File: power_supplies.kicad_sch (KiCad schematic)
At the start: 55 parts, among them IC1 ECP5-BGA256, Q16 2NPN, U15 1V8REG, U3 3V3REG, U4 1V15REG, U5 2V5REG

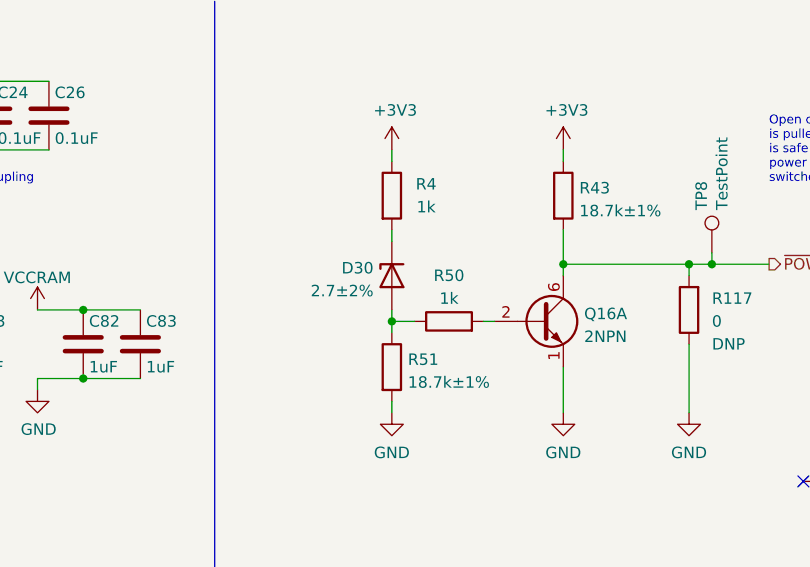
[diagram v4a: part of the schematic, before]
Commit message: Tune POWER_GOOD detection
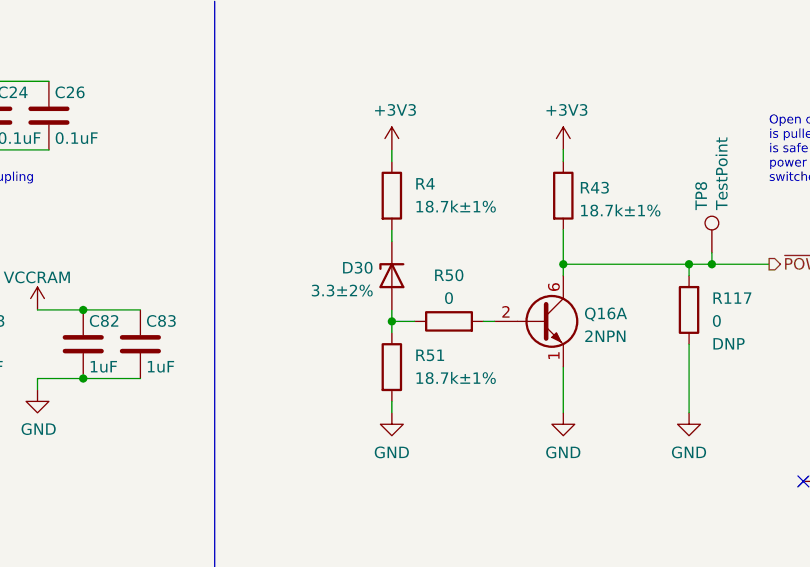
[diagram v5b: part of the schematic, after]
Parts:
- D30: value 2.7±2% -> 3.3±2%; Part Number BZX884-B2V7,315 -> BZX884-B3V3,315
- R4: value 1k -> 18.7k±1%; Manufacturer Yageo -> Panasonic; Part Number RC0402JR-071KL -> ERJ-2RKF1872X
- R50: value 1k -> 0; Part Number RC0402JR-071KL -> RC0402FR-070RL
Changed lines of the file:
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@@
       (effects (font (size 1.27 1.27)))
     )
-    (property "Value" "1k" (at 168.91 45.72 90)
+    (property "Value" "0" (at 168.91 45.72 90)
       (effects (font (size 1.27 1.27)))
     )
@@
       (effects (font (size 1.27 1.27)) hide)
     )
-    (property "Part Number" "RC0402JR-071KL" (at 168.91 48.26 0)
+    (property "Part Number" "RC0402FR-070RL" (at 168.91 48.26 0)
       (effects (font (size 1.27 1.27)) hide)
     )
@@
       (effects (font (size 1.27 1.27)) hide)
     )
-    (property "Description" "RES 1K OHM 5% 1/16W 0402" (at 168.91 48.26 0)
+    (property "Description" "RES 0 OHM JUMPER 1/16W 0402" (at 168.91 48.26 0)
       (effects (font (size 1.27 1.27)) hide)
     )
@@
       (effects (font (size 1.27 1.27)) (justify left))
     )
-    (property "Value" "2.7±2%" (at 160.528 44.8822 90)
+    (property "Value" "3.3±2%" (at 160.528 44.8822 90)
       (effects (font (size 1.27 1.27)) (justify left))
     )
@@
       (effects (font (size 1.27 1.27)) hide)
     )
-    (property "Part Number" "BZX884-B2V7,315" (at 162.56 43.18 90)
-      (effects (font (size 1.27 1.27)) hide)
-    )
-    (property "Description" "DIODE ZENER 2.7V 250MW DFN1006-2" (at 162.56 43.18 0)
+    (property "Part Number" "BZX884-B3V3,315" (at 162.56 43.18 90)
+      (effects (font (size 1.27 1.27)) hide)
+    )
+    (property "Description" "DIODE ZENER 3.3V 250MW DFN1006-2" (at 162.56 43.18 0)
       (effects (font (size 1.27 1.27)) hide)
     )
@@
   (symbol (lib_id "Device:R") (at 162.56 34.29 0) (unit 1)
     (in_bom yes) (on_board yes) (dnp no)
-    (property "Reference" "R4" (at 166.37 33.02 0)
-      (effects (font (size 1.27 1.27)))
-    )
-    (property "Value" "1k" (at 166.37 35.56 0)
-      (effects (font (size 1.27 1.27)))
+    (property "Reference" "R4" (at 165.1 33.02 0)
+      (effects (font (size 1.27 1.27)) (justify left))
+    )
+    (property "Value" "18.7k±1%" (at 165.1 35.56 0)
+      (effects (font (size 1.27 1.27)) (justify left))
     )
     (property "Footprint" "Resistor_SMD:R_0402_1005Metric" (at 160.782 34.29 90)
@@
       (effects (font (size 1.27 1.27)) hide)
     )
-    (property "Part Number" "RC0402JR-071KL" (at 162.56 34.29 0)
+    (property "Part Number" "ERJ-2RKF1872X" (at 162.56 34.29 0)
       (effects (font (size 1.27 1.27)) hide)
     )
@@
       (effects (font (size 1.27 1.27)) hide)
     )
-    (property "Description" "RES 1K OHM 5% 1/16W 0402" (at 162.56 34.29 0)
-      (effects (font (size 1.27 1.27)) hide)
-    )
-    (property "Manufacturer" "Yageo" (at 162.56 34.29 0)
+    (property "Description" "RES SMD 18.7K OHM 1% 1/10W 0402" (at 162.56 34.29 0)
+      (effects (font (size 1.27 1.27)) hide)
+    )
+    (property "Manufacturer" "Panasonic" (at 162.56 34.29 0)
       (effects (font (size 1.27 1.27)) hide)
     )
@@
   (symbol (lib_id "Device:R") (at 162.56 53.34 0) (unit 1)
     (in_bom yes) (on_board yes) (dnp no)
-    (property "Reference" "R51" (at 164.338 52.5053 0)
-      (effects (font (size 1.27 1.27)) (justify left))
-    )
-    (property "Value" "18.7k±1%" (at 164.338 55.0422 0)
-      (effects (font (size 1.27 1.27)) (justify left))
-    )
+    (property "Reference" "R51" (at 165.1 52.07 0)
+      (effects (font (size 1.27 1.27)) (justify left))
+    )
+    (property "Value" "18.7k±1%" (at 165.1 54.61 0)
+      (effects (font (size 1.27 1.27)) (justify left))
+    )

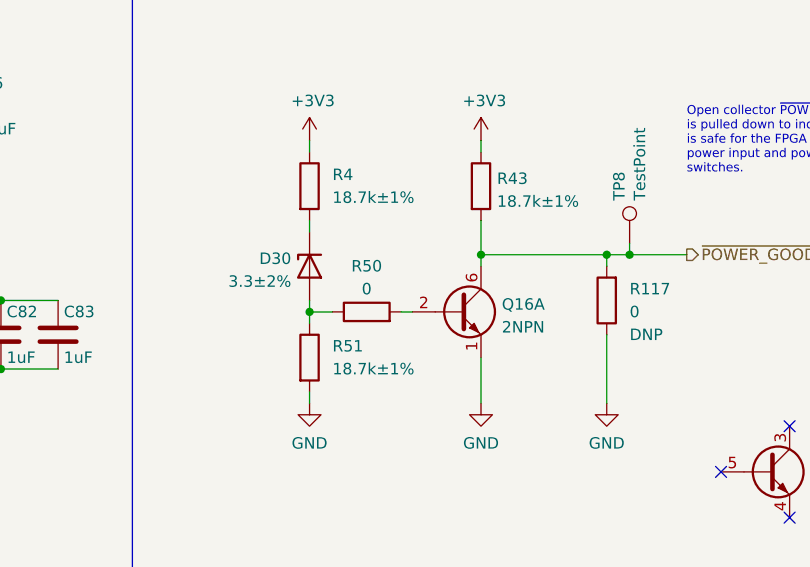
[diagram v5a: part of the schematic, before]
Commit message: Increase POWER_GOOD detection current
This helps ensure that POWER_GOOD is pulled down with sufficient
strength.
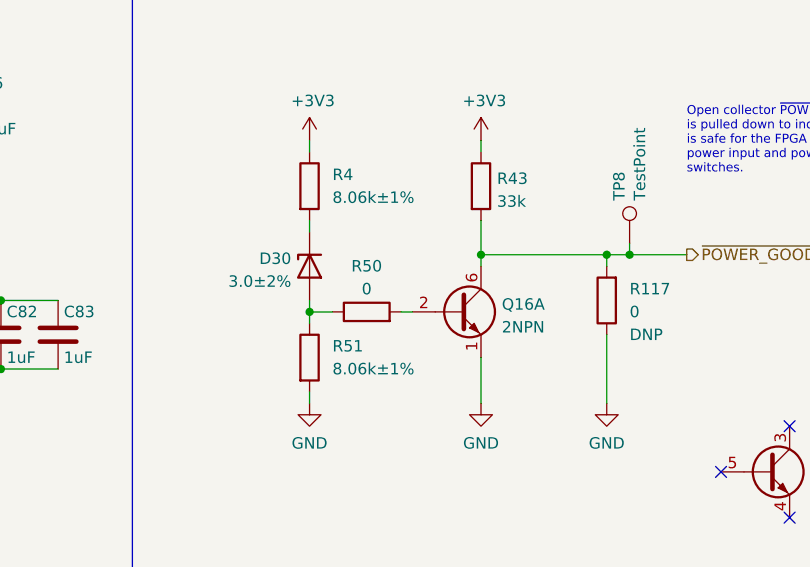
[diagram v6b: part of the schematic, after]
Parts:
- D30: value 3.3±2% -> 3.0±2%; Part Number BZX884-B3V3,315 -> BZX884-B3V0,315
- R4, R51: value 18.7k±1% -> 8.06k±1%; Part Number ERJ-2RKF1872X -> ERJ-2RKF8061X
- R43: value 18.7k±1% -> 33k; Part Number ERJ-2RKF1872X -> ERJ-2GEJ333X
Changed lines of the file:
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@@
       (effects (font (size 1.27 1.27)) (justify left))
     )
-    (property "Value" "3.3±2%" (at 160.528 44.8822 90)
+    (property "Value" "3.0±2%" (at 160.528 44.8822 90)
       (effects (font (size 1.27 1.27)) (justify left))
     )
@@
       (effects (font (size 1.27 1.27)) hide)
     )
-    (property "Part Number" "BZX884-B3V3,315" (at 162.56 43.18 90)
-      (effects (font (size 1.27 1.27)) hide)
-    )
-    (property "Description" "DIODE ZENER 3.3V 250MW DFN1006-2" (at 162.56 43.18 0)
+    (property "Part Number" "BZX884-B3V0,315" (at 162.56 43.18 90)
+      (effects (font (size 1.27 1.27)) hide)
+    )
+    (property "Description" "DIODE ZENER 3V 250MW DFN1006-2" (at 162.56 43.18 0)
       (effects (font (size 1.27 1.27)) hide)
     )
@@
       (effects (font (size 1.27 1.27)) (justify left))
     )
-    (property "Value" "18.7k±1%" (at 165.1 35.56 0)
+    (property "Value" "8.06k±1%" (at 165.1 35.56 0)
       (effects (font (size 1.27 1.27)) (justify left))
     )
@@
       (effects (font (size 1.27 1.27)) hide)
     )
-    (property "Part Number" "ERJ-2RKF1872X" (at 162.56 34.29 0)
+    (property "Part Number" "ERJ-2RKF8061X" (at 162.56 34.29 0)
       (effects (font (size 1.27 1.27)) hide)
     )
@@
       (effects (font (size 1.27 1.27)) hide)
     )
-    (property "Description" "RES SMD 18.7K OHM 1% 1/10W 0402" (at 162.56 34.29 0)
+    (property "Description" "RES SMD 8.06K OHM 1% 1/10W 0402" (at 162.56 34.29 0)
       (effects (font (size 1.27 1.27)) hide)
     )
@@
       (effects (font (size 1.27 1.27)) (justify left))
     )
-    (property "Value" "18.7k±1%" (at 165.1 54.61 0)
+    (property "Value" "8.06k±1%" (at 165.1 54.61 0)
       (effects (font (size 1.27 1.27)) (justify left))
     )
@@
       (effects (font (size 1.27 1.27)) hide)
     )
-    (property "Description" "RES SMD 18.7K OHM 1% 1/10W 0402" (at 162.56 53.34 0)
+    (property "Description" "RES SMD 8.06K OHM 1% 1/10W 0402" (at 162.56 53.34 0)
       (effects (font (size 1.27 1.27)) hide)
     )
@@
       (effects (font (size 1.27 1.27)) hide)
     )
-    (property "Part Number" "ERJ-2RKF1872X" (at 162.56 53.34 0)
+    (property "Part Number" "ERJ-2RKF8061X" (at 162.56 53.34 0)
       (effects (font (size 1.27 1.27)) hide)
     )
@@
       (effects (font (size 1.27 1.27)) (justify left))
     )
-    (property "Value" "18.7k±1%" (at 183.388 35.9922 0)
+    (property "Value" "33k" (at 183.388 35.9922 0)
       (effects (font (size 1.27 1.27)) (justify left))
     )
@@
       (effects (font (size 1.27 1.27)) hide)
     )
-    (property "Description" "RES SMD 18.7K OHM 1% 1/10W 0402" (at 181.61 34.29 0)
+    (property "Description" "RES SMD 33K OHM 5% 1/10W 0402" (at 181.61 34.29 0)
       (effects (font (size 1.27 1.27)) hide)
     )
@@
       (effects (font (size 1.27 1.27)) hide)
     )
-    (property "Part Number" "ERJ-2RKF1872X" (at 181.61 34.29 0)
-      (effects (font (size 1.27 1.27)) hide)
-    )
+    (property "Part Number" "ERJ-2GEJ333X" (at 181.61 34.29 0)
+      (effects (font (size 1.27 1.27)) hide)
+    )

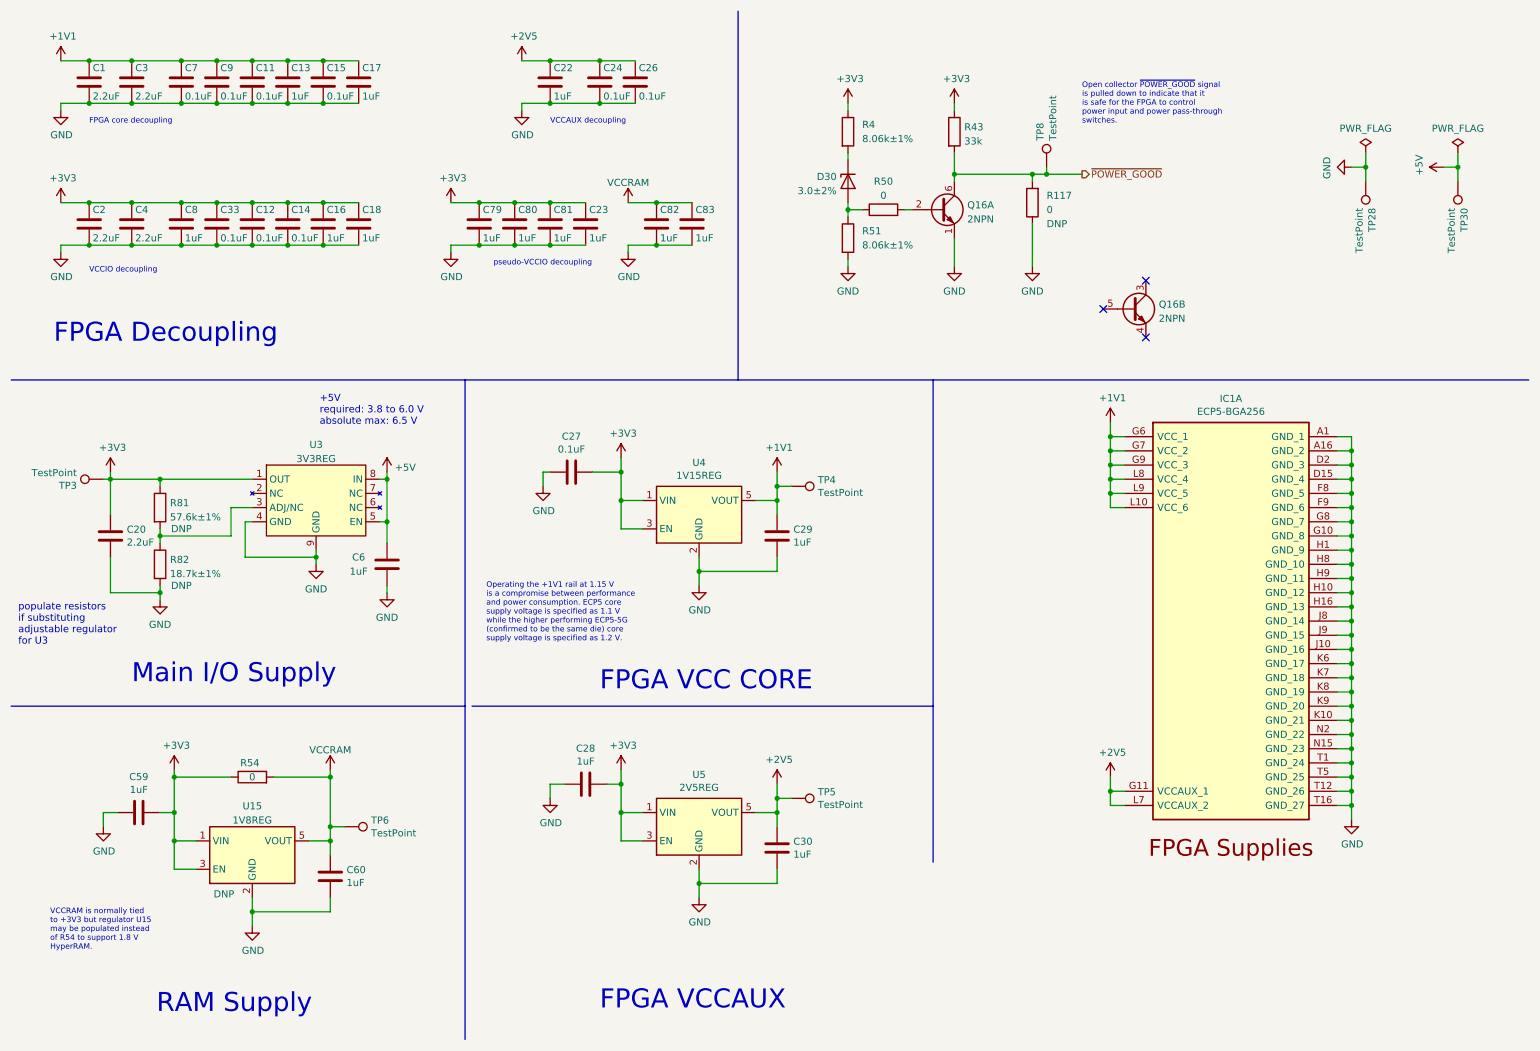
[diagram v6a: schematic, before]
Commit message: Clean up schematic
- Renumber Pmod signal names to match silkscreen labels
- Clean up FPGA symbol
- Clean up PHY symbol
- Add title block to newer sheets
- Fix horizontal line in LED sheet
- Improve various label positions
- Update data sheet fields
- Renumber pages
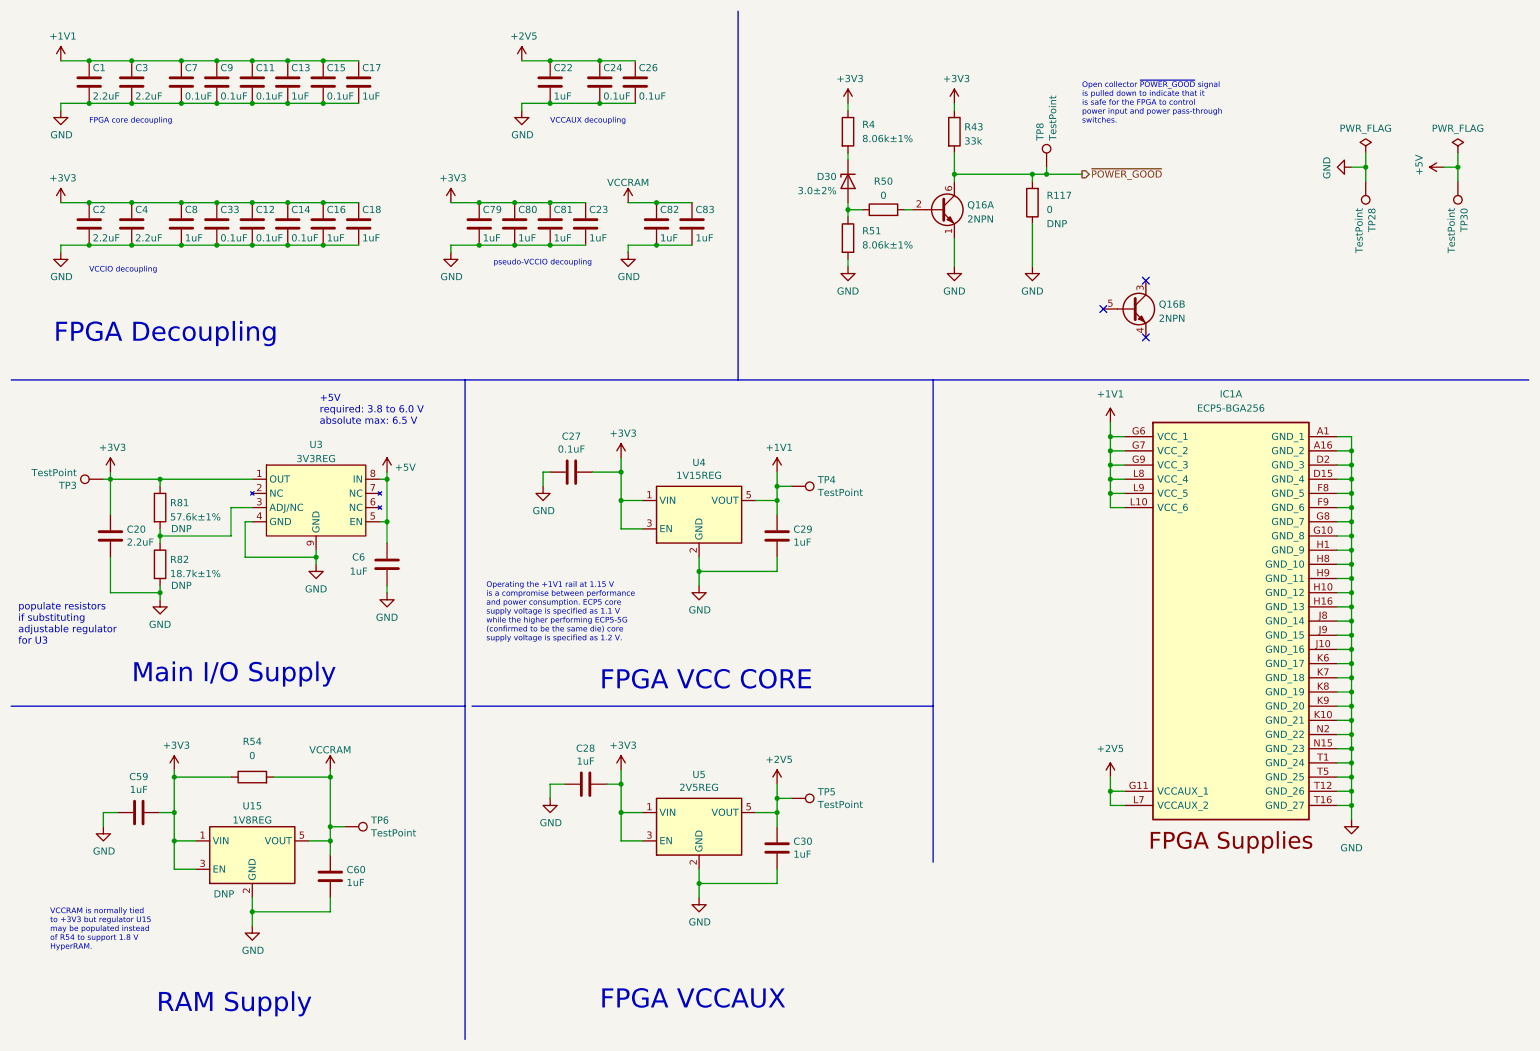
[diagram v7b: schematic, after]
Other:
- moved on the sheet: IC1A
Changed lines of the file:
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@@
     (effects (font (size 1.27 1.27)) (justify left))
   )
-  (symbol (lib_id "fpgas_and_processors:ECP5-BGA256") (at 212.09 86.36 0) (unit 1)
-    (in_bom yes) (on_board yes) (dnp no)
-    (property "Reference" "IC1" (at 231.14 82.0928 0)
+  (symbol (lib_id "fpgas_and_processors:ECP5-BGA256") (at 231.14 121.92 0) (unit 1)
+    (in_bom yes) (on_board yes) (dnp no) (fields_autoplaced)
+    (property "Reference" "IC1" (at 231.14 81.28 0)
       (effects (font (size 1.27 1.27)))
     )
-    (property "Value" "ECP5-BGA256" (at 231.14 84.4042 0)
+    (property "Value" "ECP5-BGA256" (at 231.14 83.82 0)
       (effects (font (size 1.27 1.27)))
     )
-    (property "Footprint" "cynthion:lattice_cabga256" (at 130.81 -1.27 0)
+    (property "Footprint" "cynthion:lattice_cabga256" (at 149.86 34.29 0)
       (effects (font (size 1.27 1.27)) (justify left) hide)
     )
-    (property "Datasheet" "" (at 119.38 -25.4 0)
+    (property "Datasheet" "https://www.latticesemi.com/-/media/LatticeSemi/Documents/DataSheets/ECP5/FPGA-DS-02012-2-2-ECP5-ECP5G-Family-Data-Sheet.ashx?document_id=50461" (at 138.43 10.16 0)
       (effects (font (size 1.27 1.27)) (justify left) hide)
     )
-    (property "Description" "FPGA - Field Programmable Gate Array ECP5; 12k LUTs; 1.1V" (at 119.38 -22.86 0)
+    (property "Description" "FPGA - Field Programmable Gate Array ECP5; 12k LUTs; 1.1V" (at 138.43 12.7 0)
       (effects (font (size 1.27 1.27)) (justify left) hide)
     )
-    (property "Manufacturer" "Lattice" (at 120.65 -46.99 0)
+    (property "Manufacturer" "Lattice" (at 139.7 -11.43 0)
       (effects (font (size 1.27 1.27)) (justify left) hide)
     )
-    (property "Part Number" "LFE5U-12F-6BG256C" (at 120.65 -44.45 0)
+    (property "Part Number" "LFE5U-12F-6BG256C" (at 139.7 -8.89 0)
       (effects (font (size 1.27 1.27)) (justify left) hide)
     )
-    (property "Substitution" "LFE5U-12F-*BG256*, LFE5U-25F-*BG256*" (at 212.09 86.36 0)
+    (property "Substitution" "LFE5U-12F-*BG256*, LFE5U-25F-*BG256*" (at 231.14 121.92 0)
       (effects (font (size 1.27 1.27)) hide)
     )
@@
   )
   (symbol (lib_id "power:GND") (at 252.73 157.48 0) (unit 1)
-    (in_bom yes) (on_board yes) (dnp no)
+    (in_bom yes) (on_board yes) (dnp no) (fields_autoplaced)
     (property "Reference" "#PWR038" (at 252.73 163.83 0)
       (effects (font (size 1.27 1.27)) hide)
     )
-    (property "Value" "GND" (at 252.857 161.8742 0)
+    (property "Value" "GND" (at 252.73 162.56 0)
       (effects (font (size 1.27 1.27)))
     )
@@
       (effects (font (size 1.27 1.27)) hide)
     )
-    (property "Value" "+2V5" (at 209.931 145.4658 0)
+    (property "Value" "+2V5" (at 209.55 144.78 0)
       (effects (font (size 1.27 1.27)))
     )
@@
   )
   (symbol (lib_id "power:+1V1") (at 209.55 86.36 0) (unit 1)
-    (in_bom yes) (on_board yes) (dnp no)
+    (in_bom yes) (on_board yes) (dnp no) (fields_autoplaced)
     (property "Reference" "#PWR036" (at 209.55 90.17 0)
       (effects (font (size 1.27 1.27)) hide)
     )
-    (property "Value" "+1V1" (at 209.931 81.9658 0)
+    (property "Value" "+1V1" (at 209.55 81.28 0)
       (effects (font (size 1.27 1.27)))
     )
@@
   )
   (symbol (lib_id "Device:R") (at 55.88 149.86 90) (unit 1)
-    (in_bom yes) (on_board yes) (dnp no)
-    (property "Reference" "R54" (at 57.15 147.32 90)
-      (effects (font (size 1.27 1.27)) (justify left))
+    (in_bom yes) (on_board yes) (dnp no) (fields_autoplaced)
+    (property "Reference" "R54" (at 55.88 143.51 90)
+      (effects (font (size 1.27 1.27)))
     )
-    (property "Value" "0" (at 55.88 149.86 90)
+    (property "Value" "0" (at 55.88 146.05 90)
       (effects (font (size 1.27 1.27)))
     )

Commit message: Update copyright notices
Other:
- company: Copyright 2019-2023 Great Scott Gadgets -> ${COPYRIGHT}
- title: Cynthion -> ${TITLE}
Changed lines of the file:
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@@
   (paper "A4")
   (title_block
-    (title "Cynthion")
+    (title "${TITLE}")
     (date "${DATE}")
     (rev "${VERSION}")
-    (company "Copyright 2019-2023 Great Scott Gadgets")
-    (comment 1 "Licensed under the CERN-OHL-P v2")
+    (company "${COPYRIGHT}")
+    (comment 1 "${LICENSE}")
   )
   (junction (at 102.87 54.61) (diameter 0) (color 0 0 0 0)
